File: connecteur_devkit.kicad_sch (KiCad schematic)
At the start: 4 parts, among them J5 DEVKIT_C2000_ROW_A, J6 DEVKIT_C2000_ROW_B, J7 ESP32_C6_DEVKITC_1_J1, J8 ESP32_C6_DEVKITC_1_J3

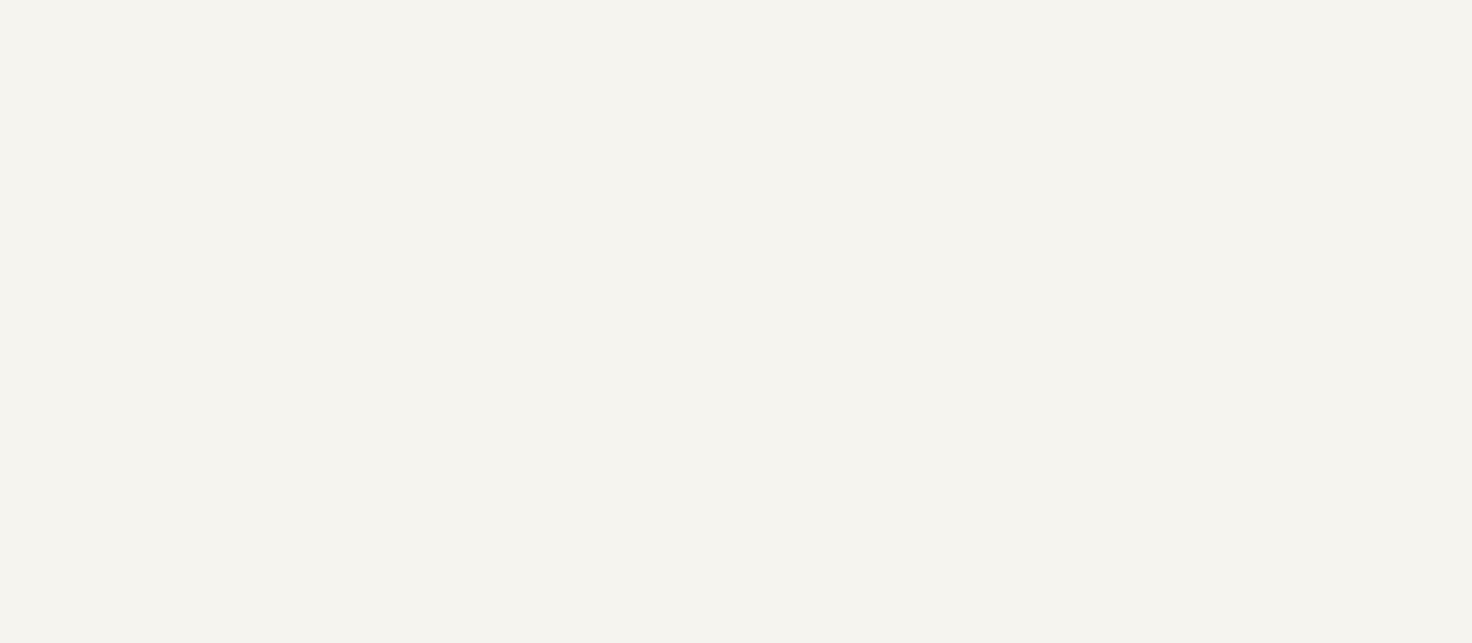
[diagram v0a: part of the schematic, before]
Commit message: Ajoute l'embase OLED (J10, IDC 2x8 detrompee) et le README du depot
Cree le symbole OLED_SPI_2x8 d'apres le plan constructeur de l'ecran
ER-OLEDM032-1B et le raccorde aux labels SPI deja presents sur les broches
natives de l'ESP32. Documente le choix dans decisions.md (#15) et
nappes-shield.md, et ajoute le README.md qui manquait a ce depot.

Co-Authored-By: Claude Sonnet 5 <noreply@anthropic.com>
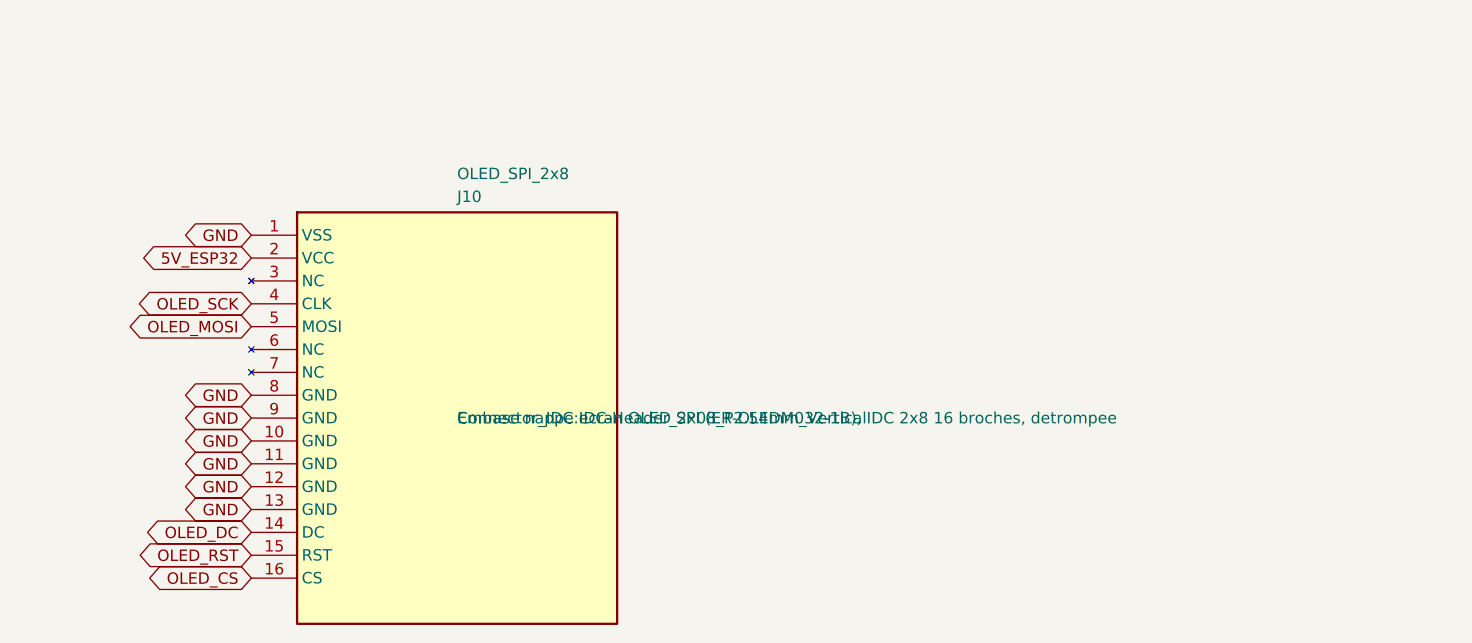
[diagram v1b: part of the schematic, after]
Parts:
- added J10: OLED_SPI_2x8, Connector_IDC:IDC-Header_2x08_P2.54mm_Vertical, symbol C2000_Devkit_Connectors:OLED_SPI_2x8
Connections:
- net 5V_ESP32: now also J10.2 (VCC)
- net GND: now also J10.1 (VSS), J10.10 (GND), J10.11 (GND), J10.12 (GND), J10.13 (GND), J10.8 (GND), J10.9 (GND)
- net OLED_CS: now also J10.16 (CS)
- net OLED_DC: now also J10.14 (DC)
- net OLED_MOSI: now also J10.5 (MOSI)
- net OLED_RST: now also J10.15 (RST)
- net OLED_SCK: now also J10.4 (CLK)

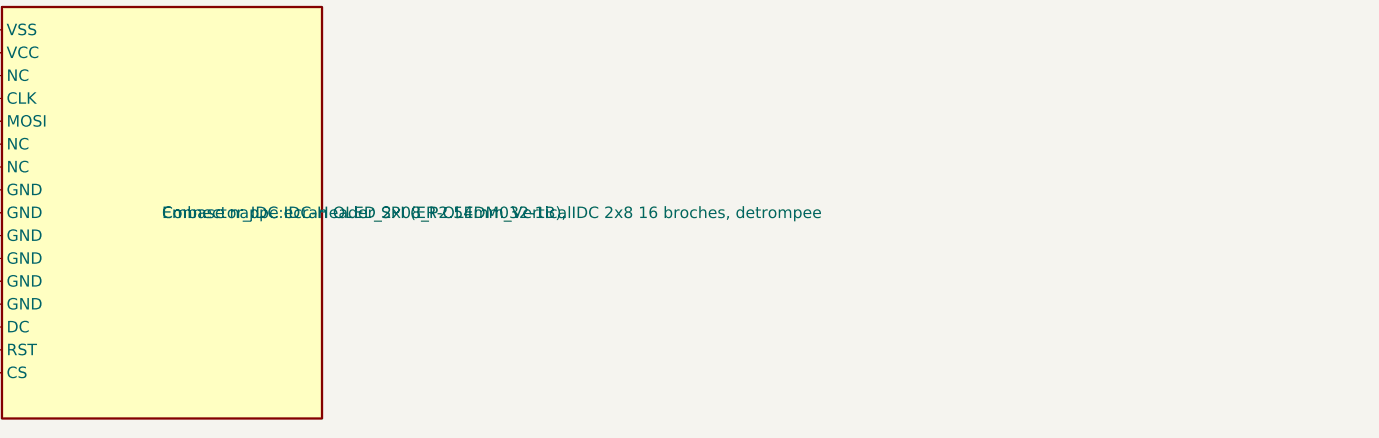
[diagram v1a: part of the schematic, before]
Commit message: Regles de clearance par domaine d'isolement et filtre EMC recommande sur les NCM3S1205MC
Ajoute deux netclasses (Isole_Primaire/Isole_Secondaire, assignees par nom
de net) et une regle shield.kicad_dru qui impose 8mm de clearance des
qu'une paire traverse les deux domaines - valeur issue du datasheet
Murata (UL62368-1, 2 MOPP, 250Vrms), pas estimee. Rien n'existait avant
pour differencier electriquement primaire et secondaire au DRC.

Ajoute le filtre EMC recommande par le datasheet (p.8) sur l'entree des
deux NCM3S1205MC (L1-L4, C26-C35), ce qui a necessite de renommer les
labels VIN_PWR/GND_PRI au niveau des pins VIN de U2/U3 vers des noeuds
intermediaires dedies (U2_VINF/U2_GNDF, U3_VINF/U3_GNDF).

Co-Authored-By: Claude Sonnet 5 <noreply@anthropic.com>
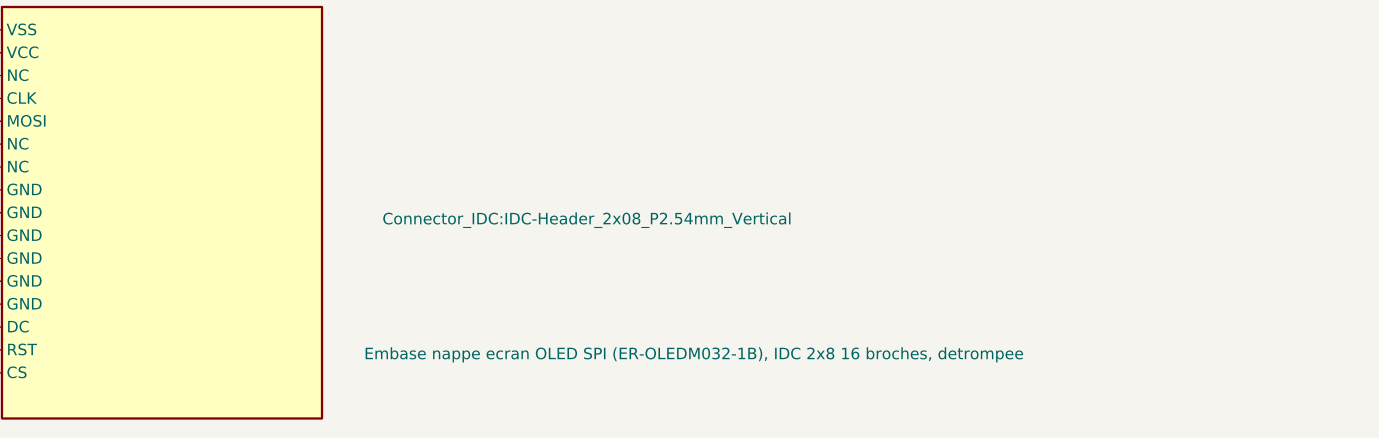
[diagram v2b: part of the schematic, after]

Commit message: Gabarit de netclasses, filtre EMC NCM3S1205MC, embase OLED, et groupement/routage des 23 trios de protection
- shield.kicad_pro : 8 netclasses (Default/Rapide/Analogique/Alim/Isole_Primaire/
  Isole_Secondaire/Puissance/HT), 83 motifs de net classes
- dc.kicad_sch : filtre EMC d'entree (L1-L4, C26-C28, C31-C33) pour les deux
  NCM3S1205MC ; etage de sortie (C4/C5 du datasheet) volontairement omis
  (decision #16, doc/decisions.md)
- connecteur_devkit.kicad_sch : embase OLED J10 (IDC 2x8 detrompee),
  symbole mecanique U4 (ER-OLEDM032-1), correction label 3V3_ESP32
- shield.kicad_pcb : les 23 trios de protection (BAT54S+R+C) groupes,
  routes (GND + signal interne), retournes en B.Cu pour matcher le
  gabarit, places en couronne hors carte pour placement/routage manuel
- doc/nappes-shield.md, doc/decisions.md : mis a jour en consequence

Co-Authored-By: Claude Sonnet 5 <noreply@anthropic.com>
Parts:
- added C36, C37: 100uF, Capacitor_SMD:C_1210_3225Metric, symbol Device:C_Polarized
- added U4: ER-OLEDM032-1, lib:ER-OLEDM032-1, symbol C2000_Devkit_Connectors:ER-OLEDM032-1
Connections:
- net 5V_C2000: now also C36.1
- net 5V_ESP32: now also C37.1; no longer J10.2 (VCC)
- net GND: now also C36.2, C37.2
- net 3V3_ESP32: now reaches J7.1 (3V3)
- net 3V3_ESP32: now also J10.2 (VCC)
